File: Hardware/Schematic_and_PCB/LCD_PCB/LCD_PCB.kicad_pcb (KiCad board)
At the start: 2 copper layers, 31.5 x 27.5 mm, 9 parts, among them J1 LCD_display, J2 Conn_01x03, J4 Conn_01x09, SW1 Button_down, SW2 Button_up, SW3 Button_ok, SW4 Button_back

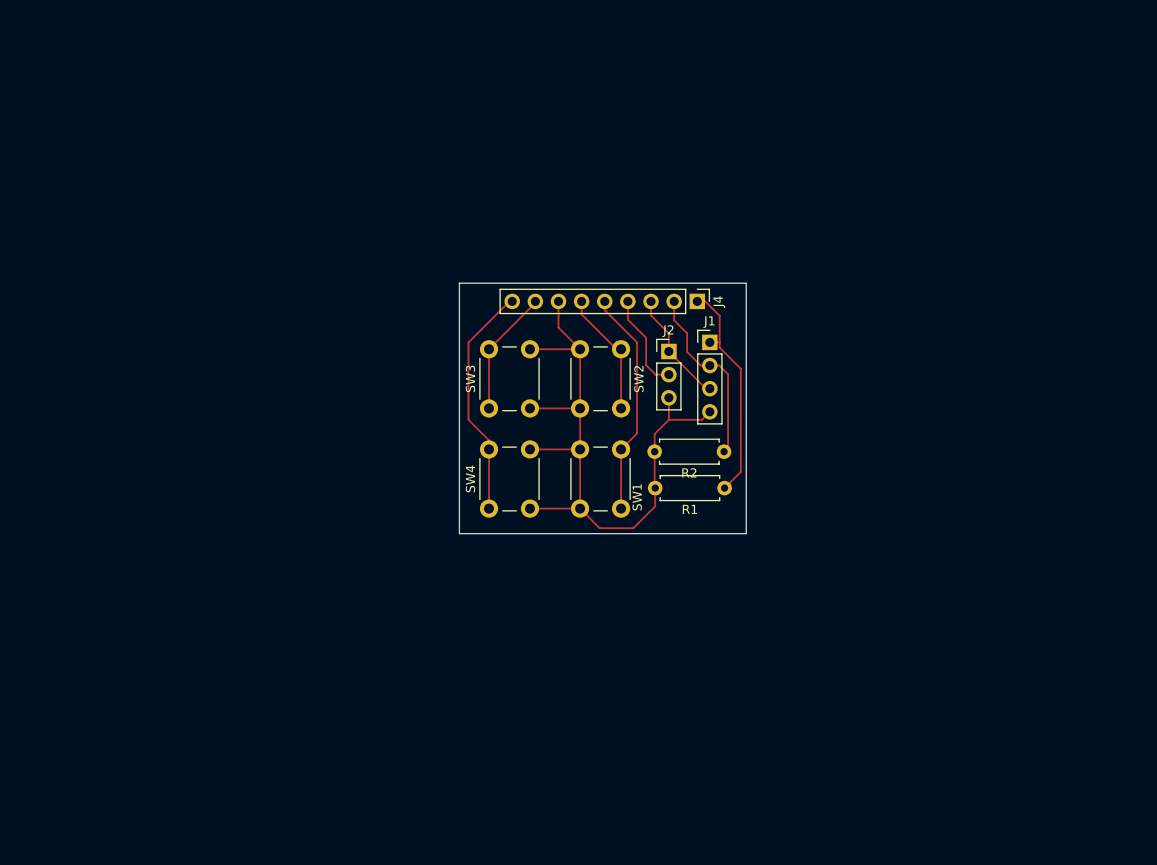
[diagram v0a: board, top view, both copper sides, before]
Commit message: Finish LCD PCB
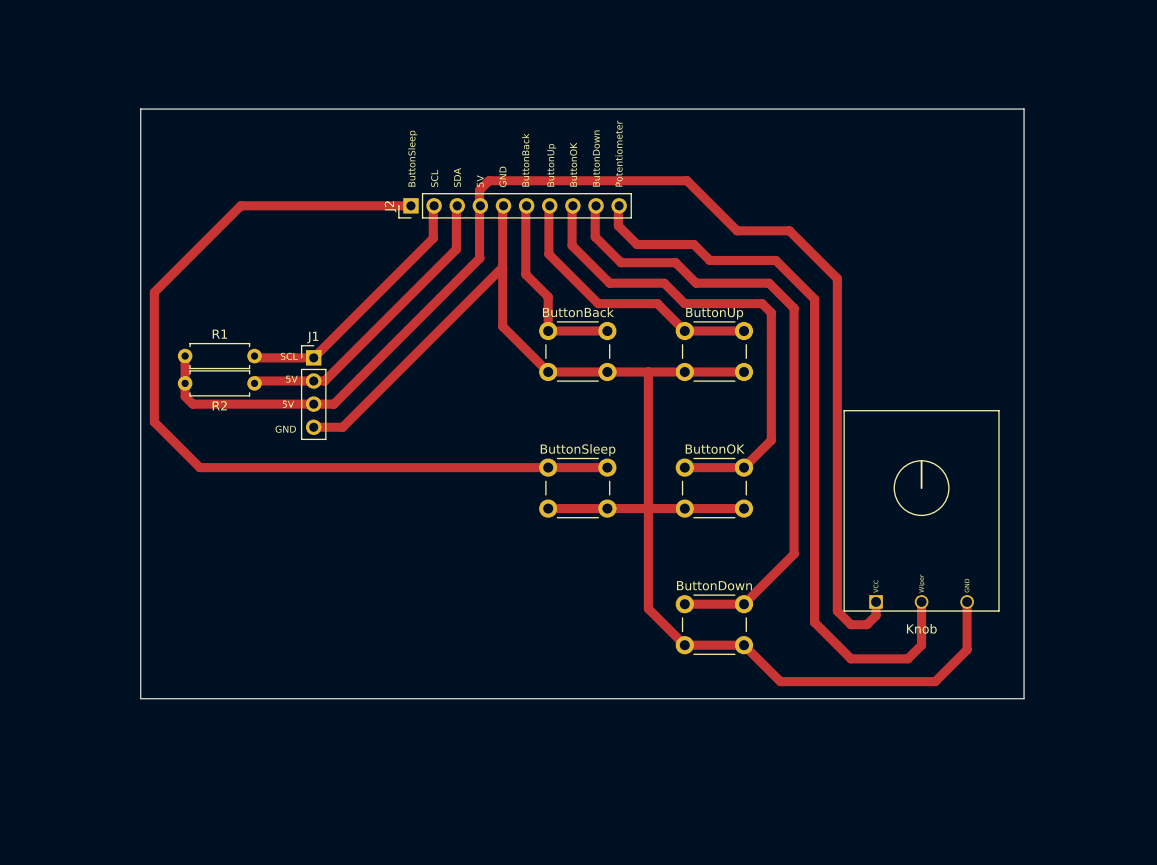
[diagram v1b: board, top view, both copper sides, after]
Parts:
- removed J4: Conn_01x09, Connector_PinHeader_2.54mm:PinHeader_1x09_P2.54mm_Vertical
- removed SW1: Button_down, Button_Switch_THT:SW_PUSH_6mm_H5mm
- removed SW2: Button_up, Button_Switch_THT:SW_PUSH_6mm_H5mm
- removed SW3: Button_ok, Button_Switch_THT:SW_PUSH_6mm_H5mm
- removed SW4: Button_back, Button_Switch_THT:SW_PUSH_6mm_H5mm
- added ButtonBack: Button_back, Button_Switch_THT:SW_PUSH_6mm_H5mm, F.Cu at (123.2, 54.8)
- added ButtonDown: Button_down, Button_Switch_THT:SW_PUSH_6mm_H5mm, F.Cu at (138.2, 84.8)
- added ButtonOK: Button_ok, Button_Switch_THT:SW_PUSH_6mm_H5mm, F.Cu at (138.2, 69.8)
- added ButtonSleep: SW_Push, Button_Switch_THT:SW_PUSH_6mm_H5mm, F.Cu at (123.2, 69.8)
- added ButtonUp: Button_up, Button_Switch_THT:SW_PUSH_6mm_H5mm, F.Cu at (138.2, 54.8)
- added Knob: Potentiometer, Potentiometer:PDB182-K-Potentiometer, F.Cu at (164.2, 84.5)
- J2: value Conn_01x03 -> Conn_01x10; footprint Connector_PinHeader_2.54mm:PinHeader_1x03_P2.54mm_Vertical -> Connector_PinHeader_2.54mm:PinHeader_1x10_P2.54mm_Vertical
- moved R1 61.0 mm to (83.4, 57.5), turned to 0 degrees
- moved R2 59.7 mm to (83.4, 60.5), turned to 0 degrees
- moved J1 43.5 mm to (97.5, 57.7)
- moved J2 32.5 mm to (108.2, 41.0), turned to 90 degrees
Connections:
- J2 pad 1: 5V -> Button Sleep
- J2 pad 2: control panel pot -> lcd SCL
- J2 pad 3: GND -> lcd SDA
- R1 pad 1: lcd SCL -> 5V
- R1 pad 2: GND -> lcd SCL
- R2 pad 1: lcd SDA -> 5V
- R2 pad 2: GND -> lcd SDA
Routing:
- net 5V: track 12.8 -> 138.7 mm
- net Button Sleep: track 0.00 -> 98.2 mm
- net GND: track 74.3 -> 162.4 mm
- net control panel pot: track 10.8 -> 81.4 mm
- net Button Down: track 24.9 -> 69.8 mm
- net Button OK: track 13.9 -> 54.0 mm
- net Button Up: track 13.8 -> 30.2 mm
- net lcd SDA: track 20.7 -> 33.0 mm
- net Button Back: track 25.8 -> 21.3 mm
- net lcd SCL: track 24.8 -> 28.7 mm
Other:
- board size 31.5 x 27.5 mm -> 97 x 64.8 mm
- board text added: "5V"
- board text added: "ButtonBack"
- board text added: "ButtonDown"
- board text added: "ButtonOK"
- board text added: "ButtonSleep"
- board text added: "ButtonUp"
- board text added: "GND"
- board text added: "Potentiometer"
- board text added: "SCL"
- board text added: "SDA"

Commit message: Update bunch of stuff
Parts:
- removed Knob: Potentiometer, Potentiometer:PDB182-K-Potentiometer
- added RV1: Control_panel_pot, Potentiometer:PDB182-K-Potentiometer-Horizontal, F.Cu at (82.8, 46.5)
- moved R1 91.2 mm to (173.0, 40.8), turned to 180 degrees
- moved R2 91.2 mm to (173.0, 43.8), turned to 180 degrees
- moved J1 66.2 mm to (161.5, 41.0)
- moved SW1 15.1 mm to (123.5, 81.5)
- moved SW2 15.1 mm to (123.5, 51.5)
- moved SW3 15.1 mm to (123.5, 66.5)
- moved SW4 15.1 mm to (108.5, 51.5)
- moved SW5 15.1 mm to (108.5, 66.5)
- moved J2 3.27 mm to (104.9, 40.8)
- renumbered ButtonDown to SW1, ButtonUp to SW2, ButtonOK to SW3, ButtonBack to SW4, ButtonSleep to SW5
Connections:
- J2 pad 1: Button Sleep -> control panel pot
- J2 pad 10: control panel pot -> lcd SDA
- J2 pad 2: lcd SCL -> 5V
- J2 pad 3: lcd SDA -> Button Sleep
- J2 pad 4: 5V -> Button Back
- J2 pad 5: GND -> Button Down
- J2 pad 6: Button Back -> Button OK
- J2 pad 8: Button OK -> GND
- J2 pad 9: Button Down -> lcd SCL
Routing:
- net Button Sleep: track 98.2 -> 38.0 mm
- net control panel pot: track 81.4 -> 24.6 mm
- net 5V: track 138.7 -> 116.8 mm
- net Button OK: track 54.0 -> 34.7 mm
- net Button Down: track 69.8 -> 50.7 mm
- net lcd SCL: track 28.7 -> 43.0 mm
- net GND: track 162.4 -> 174.9 mm
- net Button Up: track 30.2 -> 18.6 mm
- net lcd SDA: track 33.0 -> 38.8 mm
- net Button Back: track 21.3 -> 17.5 mm

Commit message: Update LCB PCB
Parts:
- J2: moved to B.Cu
- turned J2 to -90 degrees
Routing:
- net GND: track 174.9 -> 7.07 mm, vias 0 -> 1
- net 5V: track 116.8 -> 118.0 mm, vias 0 -> 2
- net Button Back: track 17.5 -> 16.8 mm, vias 0 -> 1
- net lcd SDA: track 38.8 -> 39.2 mm, vias 0 -> 1
- net lcd SCL: track 43.0 -> 43.3 mm, vias 0 -> 1
- net control panel pot: vias 0 -> 1
- net Button Up: vias 0 -> 1
- net Button Sleep: vias 0 -> 1
- net Button OK: vias 0 -> 1
- net Button Down: vias 0 -> 1
- added copper zone on F.Cu, net (none)
- added copper zone on B.Cu, net GND
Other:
- board text removed: "ButtonBack"
- board text removed: "ButtonDown"
- board text removed: "ButtonOK"
- board text removed: "ButtonSleep"
- board text removed: "ButtonUp"
- board text removed: "Potentiometer"
- board text removed: "SDA"

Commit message: Finalize LCD PCB
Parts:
- added H1: MountingHole, MountingHole:MountingHole_3.2mm_M3, F.Cu at (94.0, 36.6)
- added H2: MountingHole, MountingHole:MountingHole_3.2mm_M3, F.Cu at (140.4, 36.6)
- added H3: MountingHole, MountingHole:MountingHole_3.2mm_M3, F.Cu at (94.1, 87.9)
- added H4: MountingHole, MountingHole:MountingHole_3.2mm_M3, F.Cu at (140.4, 88.0)
- J1: moved to B.Cu
- moved R1 42.3 mm to (134.3, 57.9), turned to 90 degrees
- moved R2 37.9 mm to (137.8, 57.9), turned to 90 degrees
- moved J1 29.4 mm to (132.2, 43.5)
- moved RV1 12.1 mm to (94.0, 51.0)
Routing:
- net 5V: track 118.0 -> 78.4 mm
- net lcd SCL: track 43.3 -> 17.2 mm
- net lcd SDA: track 39.2 -> 17.2 mm
- net control panel pot: track 24.6 -> 15.2 mm
- net GND: track 7.07 -> 13.6 mm, vias 1 -> 2
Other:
- board size 97 x 64.8 mm -> 55 x 60 mm
- board text removed: "5V"
- board text removed: "GND"
- board text removed: "SCL"

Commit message: Code update for room 3
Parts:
- added TP1: TestPoint, TestPoint:TestPoint_Pad_1.5x1.5mm, F.Cu at (102.3, 55.8)
- added TP2: TestPoint, TestPoint:TestPoint_Pad_1.5x1.5mm, F.Cu at (100.5, 44.9)
- added TP3: TestPoint, TestPoint:TestPoint_Pad_1.5x1.5mm, F.Cu at (128.8, 44.0)
- added TP4: TestPoint, TestPoint:TestPoint_Pad_1.5x1.5mm, F.Cu at (136.0, 42.7)
- added TP5: TestPoint, TestPoint:TestPoint_Pad_1.5x1.5mm, F.Cu at (126.8, 34.1)
- added TP6: TestPoint, TestPoint:TestPoint_Pad_1.5x1.5mm, F.Cu at (114.0, 36.8)
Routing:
- net GND: track 13.6 -> 18.2 mm
- net 5V: track 78.4 -> 79.0 mm

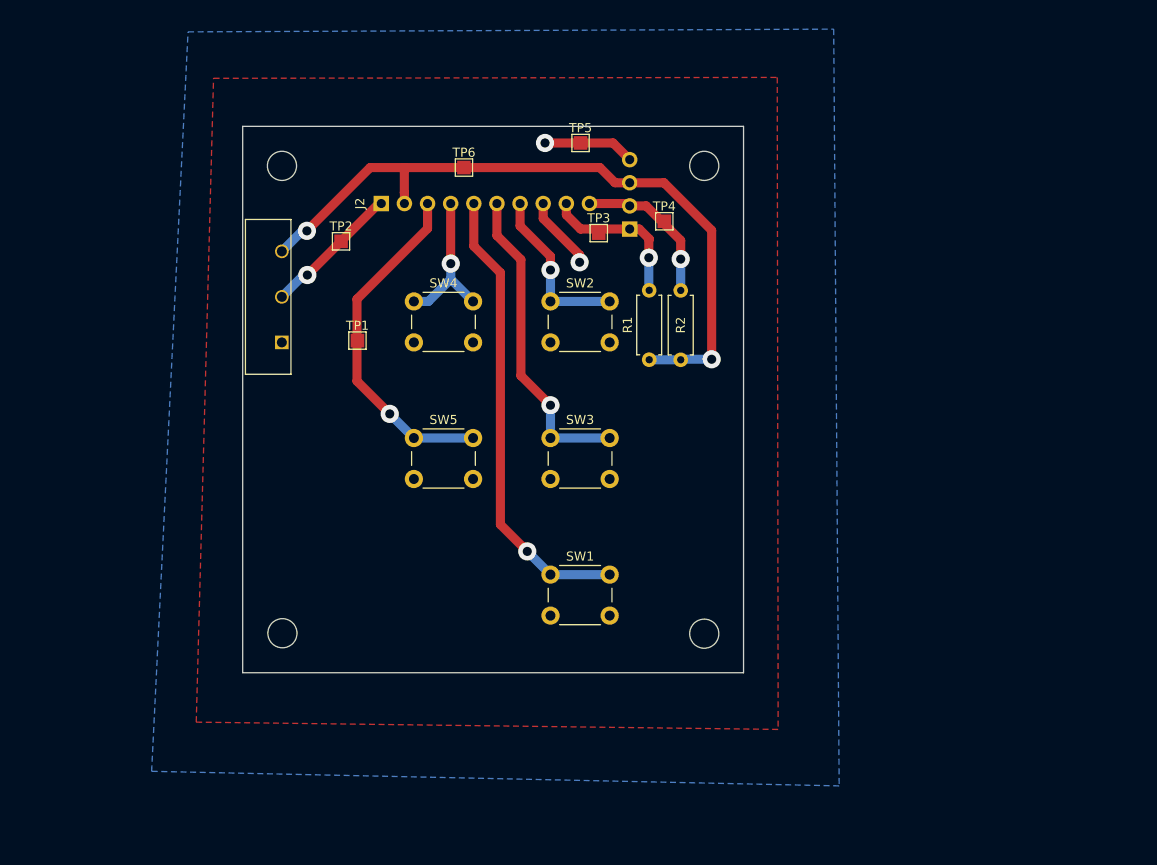
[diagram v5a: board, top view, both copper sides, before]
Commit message: LCD menu code
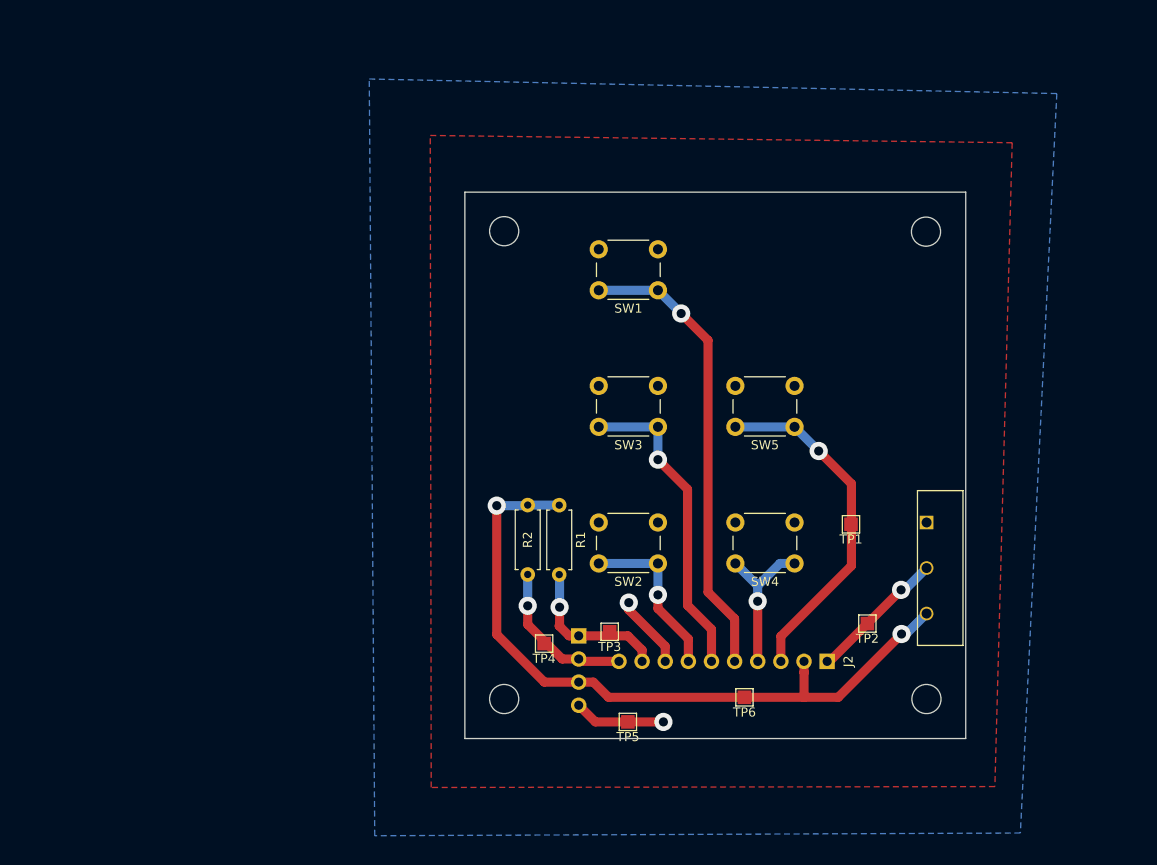
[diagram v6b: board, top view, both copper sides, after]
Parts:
- moved H1 91.9 mm to (164.8, 95.2), turned to 180 degrees
- moved H3 83.3 mm to (164.7, 43.8), turned to 180 degrees
- moved RV1 76.8 mm to (164.8, 80.8), turned to -90 degrees
- moved TP2 71.4 mm to (158.3, 86.9), turned to 180 degrees
- moved J2 70.2 mm to (153.9, 91.0), turned to 90 degrees
- moved TP6 65.8 mm to (144.8, 95.0), turned to 180 degrees
- moved TP5 63.8 mm to (132.0, 97.7), turned to 180 degrees
- moved H2 62.5 mm to (118.4, 95.2), turned to 180 degrees
- moved TP1 57.8 mm to (156.5, 76.0), turned to 180 degrees
- moved SW4 50.7 mm to (150.3, 80.3), turned to 180 degrees
- moved H4 49.4 mm to (118.4, 43.8), turned to 180 degrees
- moved TP4 48.2 mm to (122.8, 89.1), turned to 180 degrees
- moved J1 45.0 mm to (126.6, 88.2), turned to 180 degrees
- moved TP3 43.8 mm to (130.0, 87.8), turned to 180 degrees
- moved SW5 41.8 mm to (150.3, 65.3), turned to 180 degrees
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
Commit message: Update pinout order of LCD PCB
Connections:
- J2 pad 3: Button Sleep -> Button Back
- J2 pad 4: Button Back -> Button Sleep
- J2 pad 5: Button Down -> Button Up
- J2 pad 7: Button Up -> Button Down
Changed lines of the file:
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@@
 		(tags "test point SMD pad rectangle square")
 		(property "Reference" "TP2"
-			(at 0 -1.648 360)
+			(at 0 -1.648 0)
 			(layer "F.SilkS")
 			(effects
@@
 		)
 		(property "Value" "TestPoint"
-			(at 0 1.75 360)
+			(at 0 1.75 0)
 			(layer "F.Fab")
 			(effects
@@
 		)
 		(fp_text user "${REFERENCE}"
-			(at 0 -1.65 360)
+			(at 0 -1.65 0)
 			(layer "F.Fab")
 			(effects
@@
 		(tags "tact sw push 6mm")
 		(property "Reference" "SW1"
-			(at 3.25 -2 360)
+			(at 3.25 -2 0)
 			(layer "F.SilkS")
 			(effects
@@
 		)
 		(property "Value" "Button_down"
-			(at 3.75 6.7 360)
+			(at 3.75 6.7 0)
 			(layer "F.Fab")
 			(effects
@@
 		)
 		(fp_text user "${REFERENCE}"
-			(at 3.25 2.25 360)
+			(at 3.25 2.25 0)
 			(layer "F.Fab")
 			(effects
@@
 		(tags "tact sw push 6mm")
 		(property "Reference" "SW2"
-			(at 3.25 -2 360)
+			(at 3.25 -2 0)
 			(layer "F.SilkS")
 			(effects
@@
 		)
 		(property "Value" "Button_up"
-			(at 3.75 6.7 360)
+			(at 3.75 6.7 0)
 			(layer "F.Fab")
 			(effects
@@
 		)
 		(fp_text user "${REFERENCE}"
-			(at 3.25 2.25 360)
+			(at 3.25 2.25 0)
 			(layer "F.Fab")
 			(effects
@@
 		(tags "mounting hole 3.2mm no annular m3")
 		(property "Reference" "H1"
-			(at 0 -4.2 360)
+			(at 0 -4.2 0)
 			(layer "F.SilkS")
 			(hide yes)
@@
 		)
 		(property "Value" "MountingHole"
-			(at 0 4.2 360)
+			(at 0 4.2 0)
 			(layer "F.Fab")
 			(effects
@@
 		)
 		(fp_text user "${REFERENCE}"
-			(at 0 0 360)
+			(at 0 0 0)
 			(layer "F.Fab")
 			(effects
@@
 		(tags "mounting hole 3.2mm no annular m3")
 		(property "Reference" "H3"
-			(at 0 -4.2 360)
+			(at 0 -4.2 0)
 			(layer "F.SilkS")
 			(hide yes)
@@
 		)
 		(property "Value" "MountingHole"
-			(at 0 4.2 360)
+			(at 0 4.2 0)
 			(layer "F.Fab")
 			(effects
@@
 		)
 		(fp_text user "${REFERENCE}"
-			(at 0 0 360)
+			(at 0 0 0)
 			(layer "F.Fab")
 			(effects
@@
 		(tags "tact sw push 6mm")
 		(property "Reference" "SW3"
-			(at 3.25 -2 360)
+			(at 3.25 -2 0)
 			(layer "F.SilkS")
 			(effects
@@
 		)
 		(property "Value" "Button_ok"
-			(at 3.75 6.7 360)
+			(at 3.75 6.7 0)
 			(layer "F.Fab")
 			(effects
@@
 		)
 		(fp_text user "${REFERENCE}"
-			(at 3.25 2.25 360)
+			(at 3.25 2.25 0)
 			(layer "F.Fab")
 			(effects
@@
 		(tags "mounting hole 3.2mm no annular m3")
 		(property "Reference" "H4"
-			(at 0 -4.2 360)
+			(at 0 -4.2 0)
 			(layer "F.SilkS")
 			(hide yes)
@@
 		)
 		(property "Value" "MountingHole"
-			(at 0 4.2 360)
+			(at 0 4.2 0)
 			(layer "F.Fab")
 			(effects
@@
 		)
 		(fp_text user "${REFERENCE}"
-			(at 0 0 360)
+			(at 0 0 0)
 			(layer "F.Fab")
 			(effects
@@
 		(tags "mounting hole 3.2mm no annular m3")
 		(property "Reference" "H2"
-			(at 0 -4.2 360)
+			(at 0 -4.2 0)
 			(layer "F.SilkS")
 			(hide yes)
@@
 		)
 		(property "Value" "MountingHole"
-			(at 0 4.2 360)
+			(at 0 4.2 0)
 			(layer "F.Fab")
 			(effects
@@
 		)
 		(fp_text user "${REFERENCE}"
-			(at 0 0 360)
+			(at 0 0 0)
 			(layer "F.Fab")
 			(effects
@@
 		(tags "tact sw push 6mm")
 		(property "Reference" "SW5"
-			(at 3.25 -2 360)
+			(at 3.25 -2 0)
 			(layer "F.SilkS")
 			(effects
@@
 		)
 		(property "Value" "SW_Push"
-			(at 3.75 6.7 360)
+			(at 3.75 6.7 0)
 			(layer "F.Fab")
 			(effects
@@
 		)
 		(fp_text user "${REFERENCE}"
-			(at 3.25 2.25 360)
+			(at 3.25 2.25 0)
 			(layer "F.Fab")
 			(effects
@@
 		(tags "test point SMD pad rectangle square")
 		(property "Reference" "TP6"
-			(at 0 -1.648 360)
+			(at 0 -1.648 0)
 			(layer "F.SilkS")
 			(effects
@@
 		)
 		(property "Value" "TestPoint"
-			(at 0 1.75 360)
+			(at 0 1.75 0)
 			(layer "F.Fab")
 			(effects
@@
 		)
 		(fp_text user "${REFERENCE}"
-			(at 0 -1.65 360)
+			(at 0 -1.65 0)
 			(layer "F.Fab")
 			(effects
@@
 		(tags "test point SMD pad rectangle square")
 		(property "Reference" "TP4"
-			(at 0 -1.648 360)
+			(at 0 -1.648 0)
 			(layer "F.SilkS")
 			(effects
@@
 		)
 		(property "Value" "TestPoint"
-			(at 0 1.75 360)
+			(at 0 1.75 0)
 			(layer "F.Fab")
 			(effects
@@
 		)
 		(fp_text user "${REFERENCE}"
-			(at 0 -1.65 360)
+			(at 0 -1.65 0)
 			(layer "F.Fab")
 			(effects
@@
 		(tags "tact sw push 6mm")
 		(property "Reference" "SW4"
-			(at 3.25 -2 360)
+			(at 3.25 -2 0)
 			(layer "F.SilkS")
 			(effects
@@
 		)
 		(property "Value" "Button_back"
-			(at 3.75 6.7 360)
+			(at 3.75 6.7 0)
 			(layer "F.Fab")
 			(effects
@@
 		)
 		(fp_text user "${REFERENCE}"
-			(at 3.25 2.25 360)
+			(at 3.25 2.25 0)
 			(layer "F.Fab")
 			(effects
@@
 		(tags "test point SMD pad rectangle square")
 		(property "Reference" "TP3"
-			(at 0 -1.648 360)
+			(at 0 -1.648 0)
 			(layer "F.SilkS")
 			(effects
@@
 		)
 		(property "Value" "TestPoint"
-			(at 0 1.75 360)
+			(at 0 1.75 0)
 			(layer "F.Fab")
 			(effects
@@
 		)
 		(fp_text user "${REFERENCE}"
-			(at 0 -1.65 360)
+			(at 0 -1.65 0)
 			(layer "F.Fab")
 			(effects
@@
 		(tags "test point SMD pad rectangle square")
 		(property "Reference" "TP5"
-			(at 0 -1.648 360)
+			(at 0 -1.648 0)
 			(layer "F.SilkS")
 			(effects
@@
 		)
 		(property "Value" "TestPoint"
-			(at 0 1.75 360)
+			(at 0 1.75 0)
 			(layer "F.Fab")
 			(effects
@@
 		)
 		(fp_text user "${REFERENCE}"
-			(at 0 -1.65 360)
+			(at 0 -1.65 0)
 			(layer "F.Fab")
 			(effects
@@
 		(tags "test point SMD pad rectangle square")
 		(property "Reference" "TP1"
-			(at 0 -1.648 360)
+			(at 0 -1.648 0)
 			(layer "F.SilkS")
 			(effects
@@
 		)
 		(property "Value" "TestPoint"
-			(at 0 1.75 360)
+			(at 0 1.75 0)
 			(layer "F.Fab")
 			(effects
@@
 		)
 		(fp_text user "${REFERENCE}"
-			(at 0 -1.65 360)
+			(at 0 -1.65 0)
 			(layer "F.Fab")
 			(effects
@@
 		(tags "Through hole pin header THT 1x04 2.54mm single row")
 		(property "Reference" "J1"
-			(at 0 2.33 360)
+			(at 0 2.33 0)
 			(layer "B.SilkS")
 			(effects
@@
 		)
 		(property "Value" "LCD_display"
-			(at 0 -9.95 360)
+			(at 0 -9.95 0)
 			(layer "B.Fab")
 			(effects
@@
 		)
 		(fp_text user "${REFERENCE}"
-			(at 0 -11.43 360)
+			(at 0 -11.43 0)
 			(layer "B.Fab")
 			(effects
@@
 			(layers "*.Cu" "*.Mask")
 			(remove_unused_layers no)
-			(net 10 "Button Sleep")
+			(net 7 "Button Back")
 			(pinfunction "Pin_3")
 			(pintype "passive")
@@
 			(layers "*.Cu" "*.Mask")
 			(remove_unused_layers no)
-			(net 7 "Button Back")
+			(net 10 "Button Sleep")
 			(pinfunction "Pin_4")
 			(pintype "passive")
@@
 			(layers "*.Cu" "*.Mask")
 			(remove_unused_layers no)
-			(net 6 "Button Down")
+			(net 9 "Button Up")
 			(pinfunction "Pin_5")
 			(pintype "passive")
@@
 			(layers "*.Cu" "*.Mask")
 			(remove_unused_layers no)
-			(net 9 "Button Up")
+			(net 6 "Button Down")
 			(pinfunction "Pin_7")
 			(pintype "passive")
